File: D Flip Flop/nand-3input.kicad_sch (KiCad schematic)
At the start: 4 parts, among them U301 74HC00

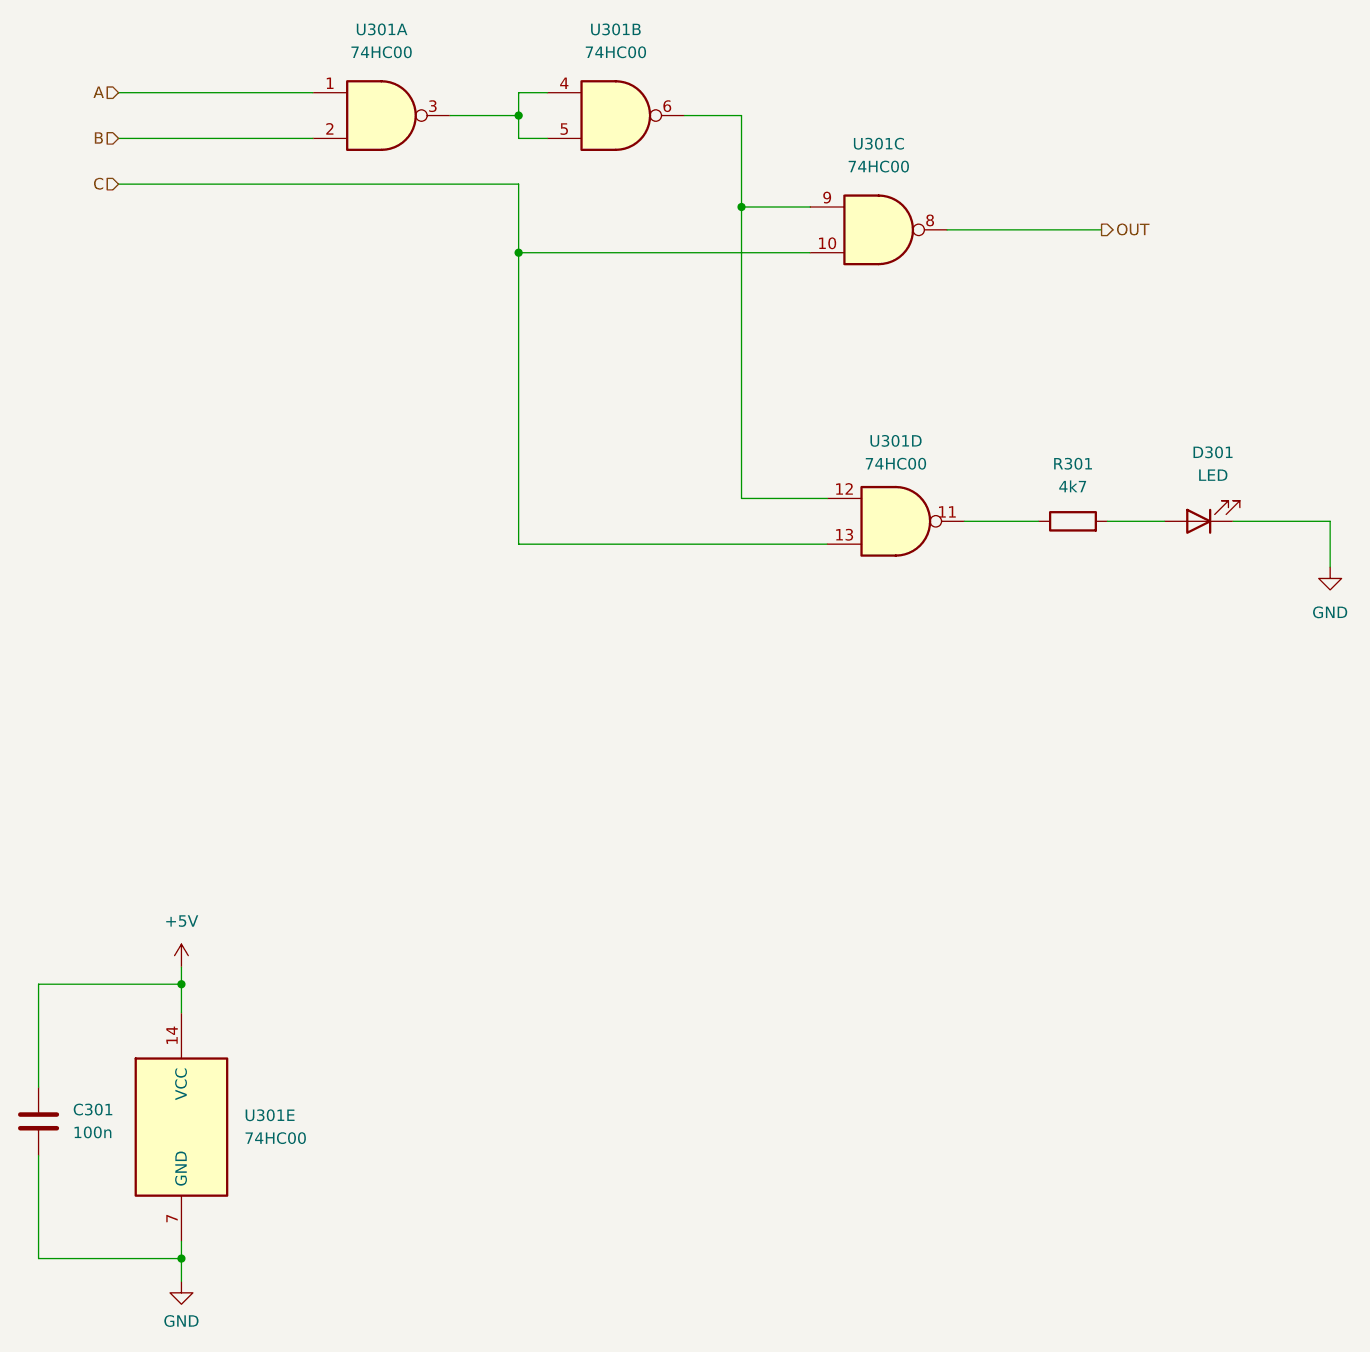
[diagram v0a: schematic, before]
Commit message: Don't need monostable for clock
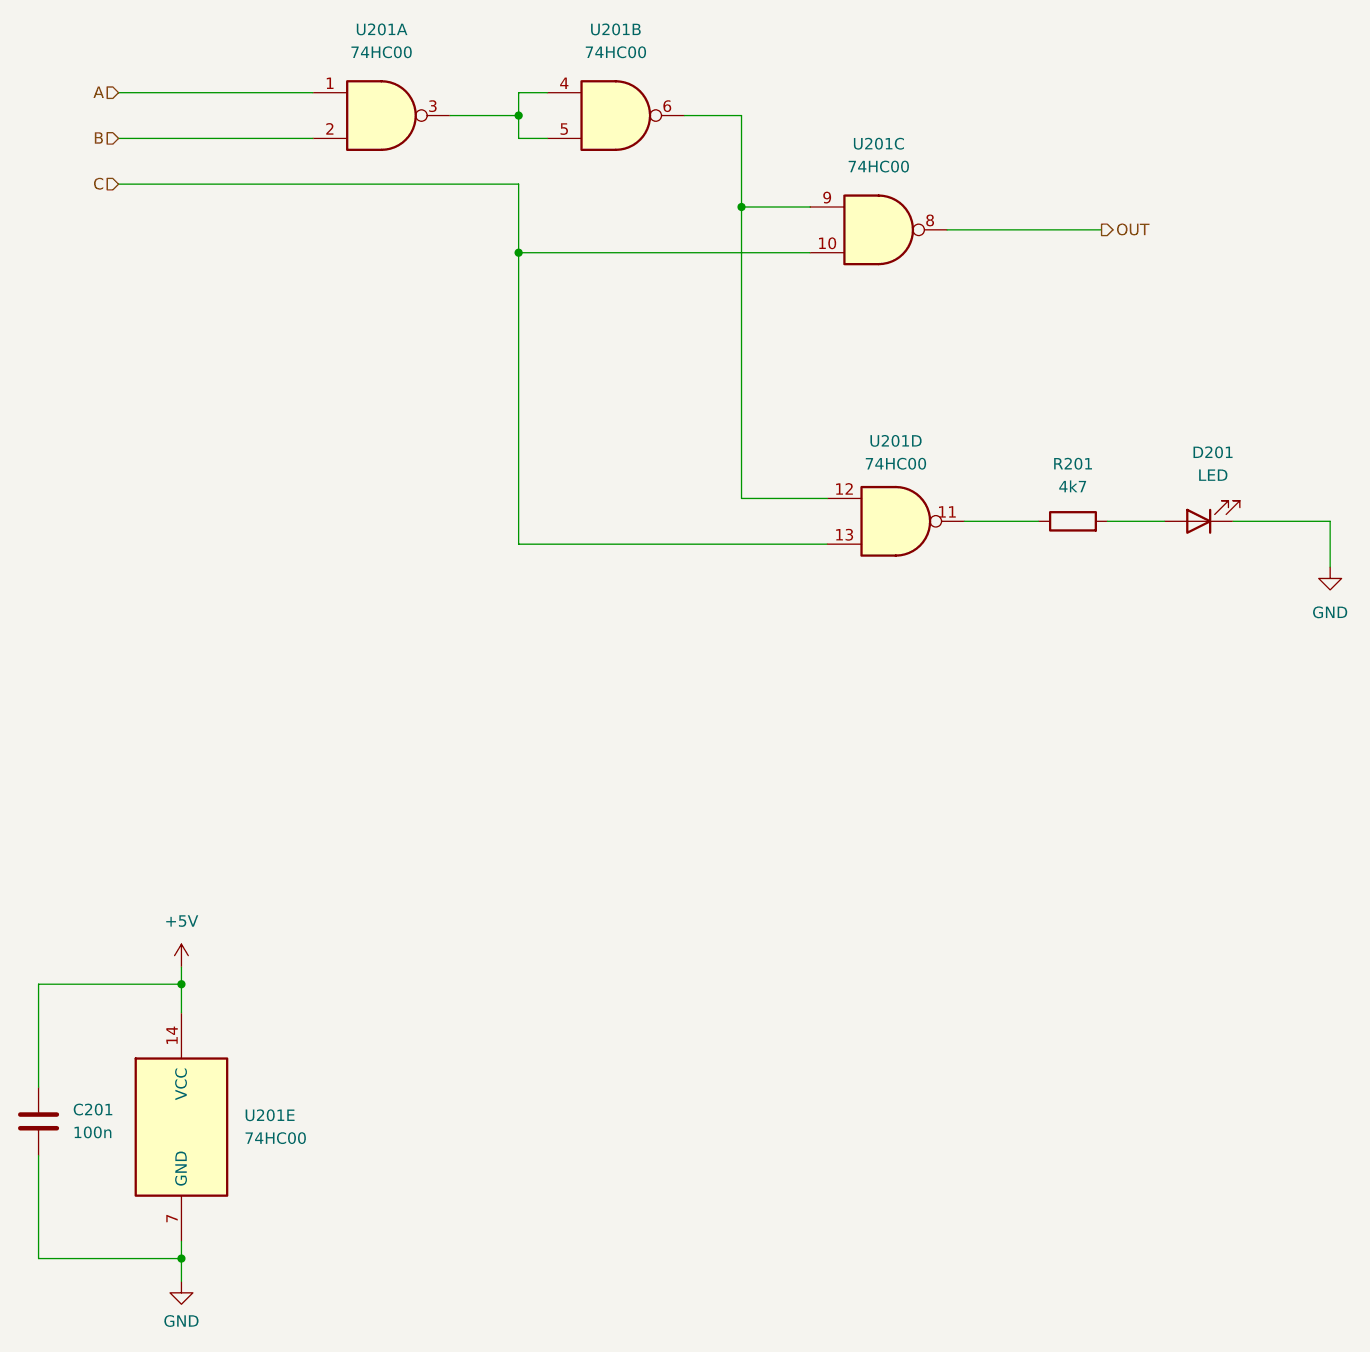
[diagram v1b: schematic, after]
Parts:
- renumbered C301 to C201, D301 to D201, R301 to R201, U301 to U201
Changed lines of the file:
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@@
   (symbol (lib_id "74xx:74HC00") (at 81.28 38.735 0) (unit 1)
     (in_bom yes) (on_board yes) (fields_autoplaced)
-    (property "Reference" "U301" (id 0) (at 81.28 29.21 0))
+    (property "Reference" "U201" (id 0) (at 81.28 29.21 0))
     (property "Value" "74HC00" (id 1) (at 81.28 31.75 0))
     (property "Footprint" "Package_DIP:DIP-14_W7.62mm_Socket" (id 2) (at 81.28 38.735 0)
@@
   (symbol (lib_id "74xx:74HC00") (at 59.055 151.13 0) (unit 5)
     (in_bom yes) (on_board yes) (fields_autoplaced)
-    (property "Reference" "U301" (id 0) (at 66.04 149.8599 0)
+    (property "Reference" "U201" (id 0) (at 66.04 149.8599 0)
       (effects (font (size 1.27 1.27)) (justify left))
     )
@@
   (symbol (lib_id "Device:R") (at 158.115 83.82 90) (unit 1)
     (in_bom yes) (on_board yes) (fields_autoplaced)
-    (property "Reference" "R301" (id 0) (at 158.115 77.47 90))
+    (property "Reference" "R201" (id 0) (at 158.115 77.47 90))
     (property "Value" "4k7" (id 1) (at 158.115 80.01 90))
     (property "Footprint" "Resistor_THT:R_Axial_DIN0207_L6.3mm_D2.5mm_P7.62mm_Horizontal" (id 2) (at 158.115 85.598 90)
@@
   (symbol (lib_id "power:+5V") (at 59.055 133.35 0) (unit 1)
     (in_bom yes) (on_board yes) (fields_autoplaced)
-    (property "Reference" "#PWR0301" (id 0) (at 59.055 137.16 0)
+    (property "Reference" "#PWR0201" (id 0) (at 59.055 137.16 0)
       (effects (font (size 1.27 1.27)) hide)
     )
@@
   (symbol (lib_id "power:GND") (at 186.69 88.9 0) (unit 1)
     (in_bom yes) (on_board yes) (fields_autoplaced)
-    (property "Reference" "#PWR0303" (id 0) (at 186.69 95.25 0)
+    (property "Reference" "#PWR0203" (id 0) (at 186.69 95.25 0)
       (effects (font (size 1.27 1.27)) hide)
     )
@@
   (symbol (lib_id "Device:C") (at 43.18 150.495 180) (unit 1)
     (in_bom yes) (on_board yes) (fields_autoplaced)
-    (property "Reference" "C301" (id 0) (at 46.99 149.2249 0)
+    (property "Reference" "C201" (id 0) (at 46.99 149.2249 0)
       (effects (font (size 1.27 1.27)) (justify right))
     )
@@
   (symbol (lib_id "power:GND") (at 59.055 168.275 0) (unit 1)
     (in_bom yes) (on_board yes) (fields_autoplaced)
-    (property "Reference" "#PWR0302" (id 0) (at 59.055 174.625 0)
+    (property "Reference" "#PWR0202" (id 0) (at 59.055 174.625 0)
       (effects (font (size 1.27 1.27)) hide)
     )
@@
   (symbol (lib_id "Device:LED") (at 172.085 83.82 180) (unit 1)
     (in_bom yes) (on_board yes) (fields_autoplaced)
-    (property "Reference" "D301" (id 0) (at 173.6725 76.2 0))
+    (property "Reference" "D201" (id 0) (at 173.6725 76.2 0))
     (property "Value" "LED" (id 1) (at 173.6725 78.74 0))
     (property "Footprint" "LED_THT:LED_D3.0mm" (id 2) (at 172.085 83.82 0)
@@
   (symbol (lib_id "74xx:74HC00") (at 138.43 83.82 0) (unit 4)
     (in_bom yes) (on_board yes) (fields_autoplaced)
-    (property "Reference" "U301" (id 0) (at 138.43 74.93 0))
+    (property "Reference" "U201" (id 0) (at 138.43 74.93 0))
     (property "Value" "74HC00" (id 1) (at 138.43 77.47 0))
     (property "Footprint" "Package_DIP:DIP-14_W7.62mm_Socket" (id 2) (at 138.43 83.82 0)
@@
   (symbol (lib_id "74xx:74HC00") (at 107.315 38.735 0) (unit 2)
     (in_bom yes) (on_board yes) (fields_autoplaced)
-    (property "Reference" "U301" (id 0) (at 107.315 29.21 0))
+    (property "Reference" "U201" (id 0) (at 107.315 29.21 0))
     (property "Value" "74HC00" (id 1) (at 107.315 31.75 0))
     (property "Footprint" "Package_DIP:DIP-14_W7.62mm_Socket" (id 2) (at 107.315 38.735 0)
@@
   (symbol (lib_id "74xx:74HC00") (at 136.525 51.435 0) (unit 3)
     (in_bom yes) (on_board yes) (fields_autoplaced)
-    (property "Reference" "U301" (id 0) (at 136.525 41.91 0))
+    (property "Reference" "U201" (id 0) (at 136.525 41.91 0))
     (property "Value" "74HC00" (id 1) (at 136.525 44.45 0))
     (property "Footprint" "Package_DIP:DIP-14_W7.62mm_Socket" (id 2) (at 136.525 51.435 0)
